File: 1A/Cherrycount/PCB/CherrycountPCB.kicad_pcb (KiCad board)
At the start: 2 copper layers, 105.4 x 64.8 mm, 22 parts, among them J1 Conn_01x02_Female, J2 Conn_01x03_Female, J3 Conn_01x05_Female, J4 Screw_Terminal_01x02, J5 Screw_Terminal_01x02, Q1 2SA1015, Q2 2SA1015

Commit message: Version finale du PCB de compteur de cerises
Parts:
- added G***: LOGO, 7seg:Logo, B.Cu at (172.7, 74.9)
- added J4: Screw_Terminal_01x02, TerminalBlock:TerminalBlock_bornier-2_P5.08mm, F.Cu at (189.2, 87.6)
- renumbered J4 to J5, J5 to J6
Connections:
- F1 pad 1: Net-(J4-Pad1) -> Net-(F1-Pad1)
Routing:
- net Net-(F1-Pad1): track 0.00 -> 15.7 mm
- net Net-(J4-Pad1): track 11.3 -> 10.8 mm
- added copper zone on B.Cu, net GND
- added copper zone on F.Cu, net GND
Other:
- board size 105.4 x 64.8 mm -> 105.4 x 66 mm
- board text added: "GND"
- board text added: "VIN"

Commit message: Version finale du PCB du compteur de cerises
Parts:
- moved A1 7.62 mm to (148.0, 115.6)
- moved AFF1 7.62 mm to (138.9, 74.6)
- moved AFF2 7.62 mm to (163.0, 74.6)
- moved D1 7.62 mm to (182.9, 118.3)
- moved G*** 7.62 mm to (180.3, 74.9)
- moved J1 7.62 mm to (130.8, 123.3)
- moved J2 7.62 mm to (115.6, 123.3)
- moved J3 7.62 mm to (143.5, 123.3)
- moved J4 7.62 mm to (196.8, 87.6)
- moved J5 7.62 mm to (195.6, 97.9)
- moved J6 7.62 mm to (195.6, 111.8)
- moved Q2 7.62 mm to (179.1, 96.0)
- moved R10 7.62 mm to (181.6, 90.0)
- moved R3 7.62 mm to (123.8, 72.5)
- moved R6 7.62 mm to (142.2, 86.7)
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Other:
- outline, holes or cut-outs redrawn

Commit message: Version finale du PCB de compteur de cerises
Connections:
- J3 pad 4: GND -> VIN
- J3 pad 5: VIN -> GND
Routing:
- net VIN: track 87.2 -> 87.8 mm
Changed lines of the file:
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@@
       (net 5 "Net-(A1-Pad5)") (pinfunction "Pin_3") (pintype "passive"))
     (pad "4" thru_hole oval (at 0 7.62 90) (size 1.7 1.7) (drill 1) (layers *.Cu *.Mask)
-      (net 6 "GND") (pinfunction "Pin_4") (pintype "passive"))
+      (net 8 "VIN") (pinfunction "Pin_4") (pintype "passive"))
     (pad "5" thru_hole oval (at 0 10.16 90) (size 1.7 1.7) (drill 1) (layers *.Cu *.Mask)
-      (net 8 "VIN") (pinfunction "Pin_5") (pintype "passive"))
+      (net 6 "GND") (pinfunction "Pin_5") (pintype "passive"))
     (model "${KICAD6_3DMODEL_DIR}/Connector_PinHeader_2.54mm.3dshapes/PinHeader_1x05_P2.54mm_Vertical.wrl"
       (offset (xyz 0 0 0))
@@
   (gr_circle (center 195.58 69.85) (end 197.08 69.85) (layer "Edge.Cuts") (width 0.1) (fill none))
   (gr_circle (center 102.87 69.85) (end 104.37 69.85) (layer "Edge.Cuts") (width 0.1) (fill none))
-  (gr_text "GND" (at 151.13 127) (layer "F.SilkS")
+  (gr_text "GND" (at 153.67 127) (layer "F.SilkS")
     (effects (font (size 0.8 0.8) (thickness 0.125)))
   )
@@
     (effects (font (size 0.8 0.8) (thickness 0.125)))
   )
-  (gr_text "VIN" (at 153.67 127) (layer "F.SilkS")
+  (gr_text "VIN" (at 151.13 127) (layer "F.SilkS")
     (effects (font (size 0.8 0.8) (thickness 0.125)))
   )
@@
   (segment (start 142.24 125.795) (end 137.795 121.35) (width 0.25) (layer "B.Cu") (net 5))
   (segment (start 137.795 121.35) (end 137.795 115.635) (width 0.25) (layer "B.Cu") (net 5))
+  (segment (start 166.305 123.255) (end 153.67 123.255) (width 0.25) (layer "F.Cu") (net 6))
   (segment (start 121.905 124.525) (end 132.08 124.525) (width 0.25) (layer "F.Cu") (net 6))
-  (segment (start 170.02 118.335) (end 182.88 118.335) (width 0.25) (layer "F.Cu") (net 6))
-  (segment (start 163.83 124.525) (end 170.02 118.335) (width 0.25) (layer "F.Cu") (net 6))
+  (segment (start 151.195 125.73) (end 153.67 123.255) (width 0.25) (layer "F.Cu") (net 6))
+  (segment (start 182.88 118.335) (end 171.225 118.335) (width 0.25) (layer "F.Cu") (net 6))
   (segment (start 135.255 121.35) (end 135.255 115.635) (width 0.25) (layer "F.Cu") (net 6))
+  (segment (start 139.635 125.73) (end 151.195 125.73) (width 0.25) (layer "F.Cu") (net 6))
   (segment (start 195.58 116.905) (end 184.31 116.905) (width 0.25) (layer "F.Cu") (net 6))
-  (segment (start 151.13 123.255) (end 152.4 124.525) (width 0.25) (layer "F.Cu") (net 6))
   (segment (start 133.35 123.255) (end 135.255 121.35) (width 0.25) (layer "F.Cu") (net 6))
   (segment (start 184.31 116.905) (end 182.88 118.335) (width 0.25) (layer "F.Cu") (net 6))
-  (segment (start 152.4 124.525) (end 163.83 124.525) (width 0.25) (layer "F.Cu") (net 6))
   (segment (start 120.635 123.255) (end 121.905 124.525) (width 0.25) (layer "F.Cu") (net 6))
   (segment (start 132.08 124.525) (end 133.35 123.255) (width 0.25) (layer "F.Cu") (net 6))
-  (segment (start 135.255 121.35) (end 138.43 124.525) (width 0.25) (layer "F.Cu") (net 6))
-  (segment (start 138.43 124.525) (end 149.86 124.525) (width 0.25) (layer "F.Cu") (net 6))
-  (segment (start 149.86 124.525) (end 151.13 123.255) (width 0.25) (layer "F.Cu") (net 6))
+  (segment (start 171.225 118.335) (end 166.305 123.255) (width 0.25) (layer "F.Cu") (net 6))
+  (segment (start 135.255 121.35) (end 139.635 125.73) (width 0.25) (layer "F.Cu") (net 6))
   (segment (start 182.88 110.715) (end 185.42 108.175) (width 0.25) (layer "F.Cu") (net 8))
-  (segment (start 161.29 115.635) (end 175.26 115.635) (width 0.25) (layer "F.Cu") (net 8))
-  (segment (start 130.175 113.73) (end 130.175 115.635) (width 0.25) (layer "F.Cu") (net 8))
-  (segment (start 130.81 113.095) (end 130.175 113.73) (width 0.25) (layer "F.Cu") (net 8))
-  (segment (start 153.67 123.255) (end 148.59 118.175) (width 0.25) (layer "F.Cu") (net 8))
+  (segment (start 134.62 113.03) (end 130.81 113.03) (width 0.25) (layer "F.Cu") (net 8))
+  (segment (start 180.565 110.715) (end 175.71 115.57) (width 0.25) (layer "F.Cu") (net 8))
+  (segment (start 136.38 114.79) (end 134.62 113.03) (width 0.25) (layer "F.Cu") (net 8))
+  (segment (start 182.88 110.715) (end 180.565 110.715) (width 0.25) (layer "F.Cu") (net 8))
+  (segment (start 175.71 115.57) (end 156.21 115.57) (width 0.25) (layer "F.Cu") (net 8))
+  (segment (start 136.38 116.100991) (end 136.38 114.79) (width 0.25) (layer "F.Cu") (net 8))
   (segment (start 121.905 119.445) (end 127 119.445) (width 0.25) (layer "F.Cu") (net 8))
-  (segment (start 134.62 113.095) (end 130.81 113.095) (width 0.25) (layer "F.Cu") (net 8))
-  (segment (start 180.18 110.715) (end 182.88 110.715) (width 0.25) (layer "F.Cu") (net 8))
+  (segment (start 151.13 120.65) (end 151.13 123.255) (width 0.25) (layer "F.Cu") (net 8))
+  (segment (start 130.175 113.665) (end 130.175 115.635) (width 0.25) (layer "F.Cu") (net 8))
+  (segment (start 151.13 120.65) (end 140.929009 120.65) (width 0.25) (layer "F.Cu") (net 8))
   (segment (start 118.095 123.255) (end 121.905 119.445) (width 0.25) (layer "F.Cu") (net 8))
-  (segment (start 175.26 115.635) (end 180.18 110.715) (width 0.25) (layer "F.Cu") (net 8))
   (segment (start 127 119.445) (end 130.175 116.27) (width 0.25) (layer "F.Cu") (net 8))
+  (segment (start 140.929009 120.65) (end 136.38 116.100991) (width 0.25) (layer "F.Cu") (net 8))
   (segment (start 185.42 108.175) (end 185.42 105.185) (width 0.25) (layer "F.Cu") (net 8))
-  (segment (start 148.59 118.175) (end 138.43 118.175) (width 0.25) (layer "F.Cu") (net 8))
-  (segment (start 136.38 116.125) (end 136.38 114.855) (width 0.25) (layer "F.Cu") (net 8))
-  (segment (start 153.67 123.255) (end 161.29 115.635) (width 0.25) (layer "F.Cu") (net 8))
-  (segment (start 138.43 118.175) (end 136.38 116.125) (width 0.25) (layer "F.Cu") (net 8))
+  (segment (start 130.81 113.03) (end 130.175 113.665) (width 0.25) (layer "F.Cu") (net 8))
+  (segment (start 156.21 115.57) (end 151.13 120.65) (width 0.25) (layer "F.Cu") (net 8))
   (segment (start 130.175 116.27) (end 130.175 115.635) (width 0.25) (layer "F.Cu") (net 8))
-  (segment (start 136.38 114.855) (end 134.62 113.095) (width 0.25) (layer "F.Cu") (net 8))
   (segment (start 116.06 122.75) (end 116.06 112.315) (width 0.25) (layer "B.Cu") (net 16))
   (segment (start 116.06 112.315) (end 102.87 99.125) (width 0.25) (layer "B.Cu") (net 16))

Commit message: Version finale du PCB de compteur de cerises
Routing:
- net D12: track 89.2 -> 90.7 mm
- net Net-(AFF1-Pad10): track 115.8 -> 116.8 mm
- net Net-(A1-Pad28): track 28.0 -> 28.9 mm
- net DP: track 41.5 -> 42.2 mm
- net Net-(AFF1-Pad6): track 56.6 -> 57.2 mm
- net GND: vias 0 -> 3

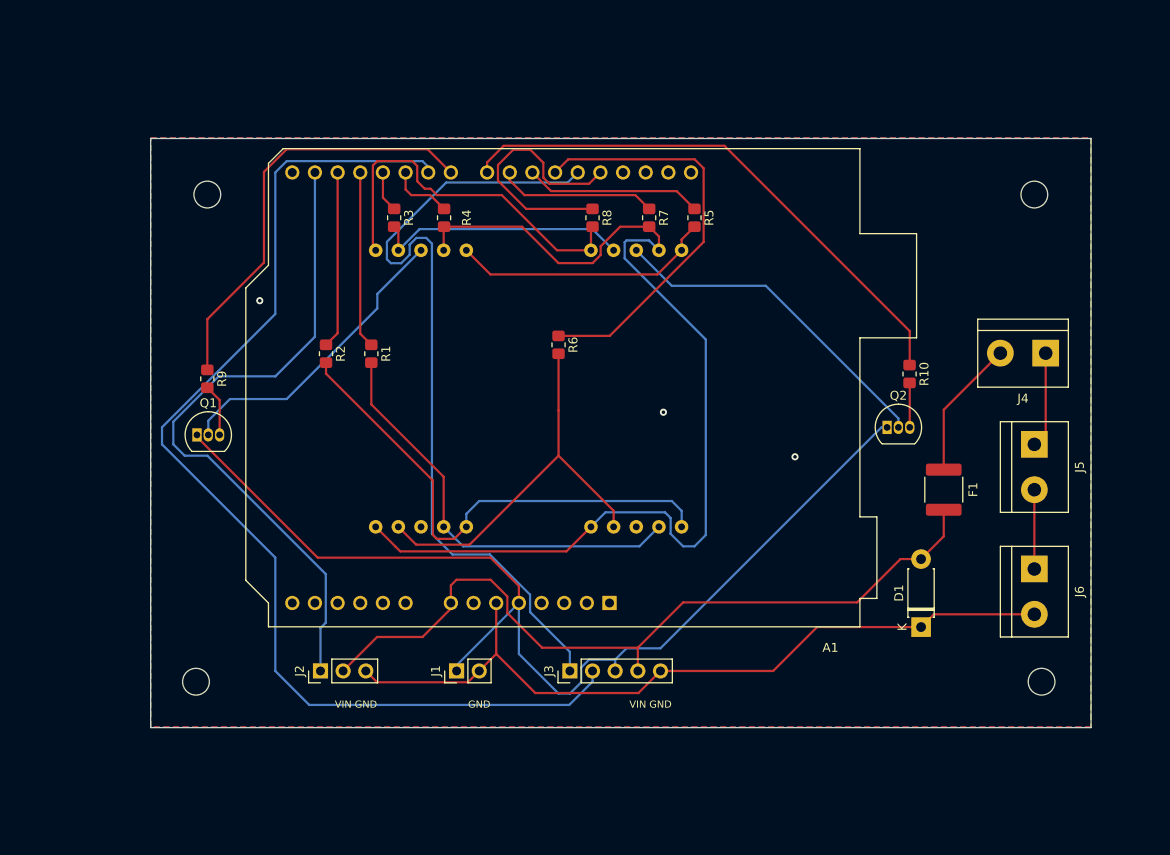
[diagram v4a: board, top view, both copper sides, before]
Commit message: Correction du code Arduino & PCB Cherrycount
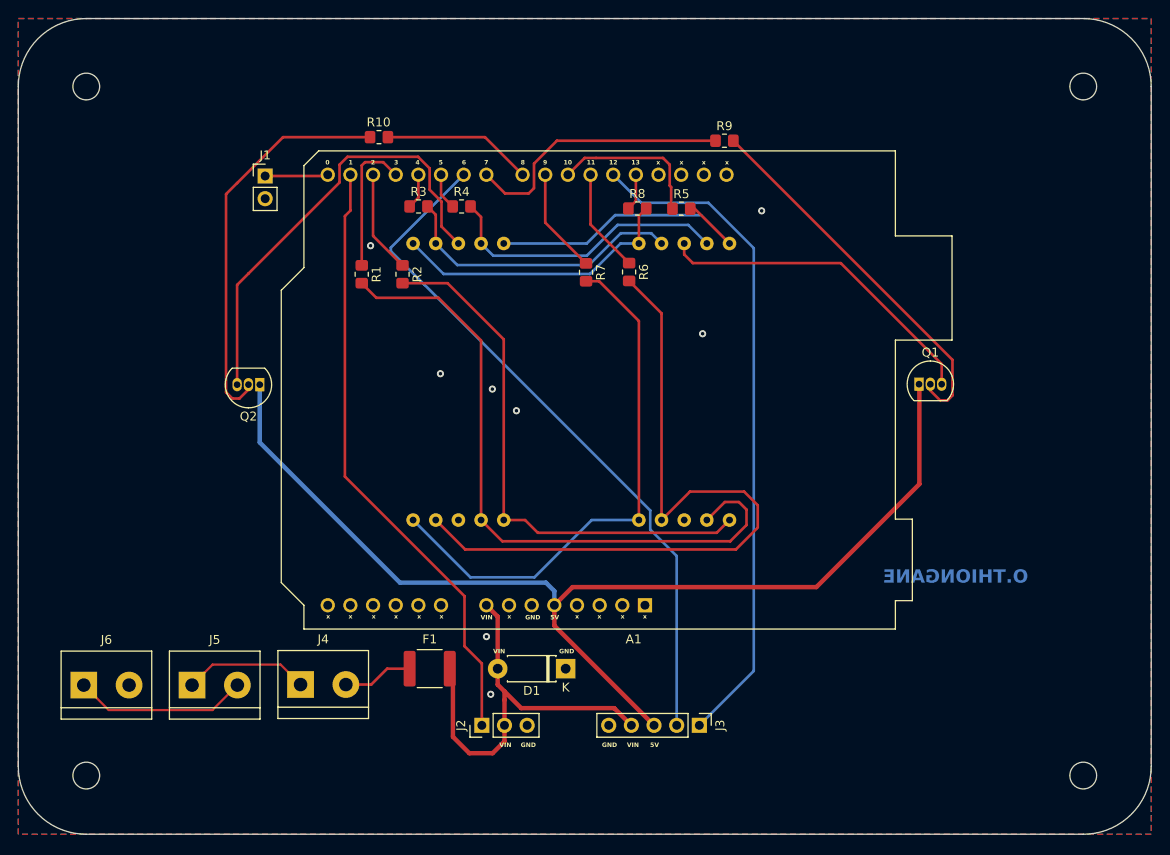
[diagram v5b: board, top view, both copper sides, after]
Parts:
- A1: value Arduino_UNO_R3 -> Arduino_Leonardo
- D1: value DIODE -> type="D" model="DIODE" lib=""
- Q1, Q2: value 2SA1015 -> S8550
- moved J6 107.4 mm to (89.0, 124.8), turned to 0 degrees
- moved J5 98.2 mm to (101.2, 124.8), turned to 0 degrees
- moved J4 91.4 mm to (113.3, 124.8), turned to 0 degrees
- moved Q1 81.1 mm to (182.7, 91.1)
- moved Q2 70.5 mm to (108.8, 91.2), turned to 180 degrees
- moved R10 65.1 mm to (122.1, 63.4), turned to 180 degrees
- moved R9 63.8 mm to (160.8, 63.8), turned to 0 degrees
- moved F1 61.0 mm to (127.8, 123.0), turned to 0 degrees
- moved J1 59.5 mm to (109.4, 67.8), turned to 0 degrees
- moved D1 40.1 mm to (143.0, 123.0), turned to 180 degrees
- moved AFF1 29.5 mm to (168.4, 73.8)
- moved AFF2 20.0 mm to (143.1, 73.8)
- moved J2 19.1 mm to (133.6, 129.3)
- moved J3 15.7 mm to (158.0, 129.3), turned to -90 degrees
- moved G*** 13.5 mm to (190.5, 66.0)
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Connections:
- A1 pad 15: unconnected-(A1-Pad15) -> Net-(A1-D0/RX)
- A1 pad 5: Net-(A1-Pad5) -> Net-(A1-+5V)
- AFF1 pad 10: Net-(AFF1-Pad10) -> Net-(AFF1-g)
- AFF1 pad 2: Net-(AFF1-Pad10) -> Net-(AFF1-d)
- AFF1 pad 3: Net-(AFF1-Pad3) -> Net-(Q1-C)
- AFF2 pad 10: Net-(AFF1-Pad10) -> Net-(AFF1-g)
- AFF2 pad 2: Net-(AFF1-Pad10) -> Net-(AFF1-d)
- AFF2 pad 3: Net-(AFF2-Pad3) -> Net-(Q2-C)
- J1 pad 1: Net-(A1-Pad5) -> Net-(A1-D0/RX)
- J3 pad 3: Net-(A1-Pad5) -> Net-(A1-+5V)
- Q1 pad 1: Net-(A1-Pad5) -> Net-(A1-+5V)
- Q1 pad 2: Net-(AFF1-Pad3) -> Net-(Q1-B)
- Q1 pad 3: Net-(Q1-Pad3) -> Net-(Q1-C)
- Q2 pad 1: Net-(A1-Pad5) -> Net-(A1-+5V)
- Q2 pad 2: Net-(AFF2-Pad3) -> Net-(Q2-B)
- Q2 pad 3: Net-(Q2-Pad3) -> Net-(Q2-C)
- R10 pad 2: Net-(Q2-Pad3) -> Net-(Q2-B)
- R4 pad 2: Net-(AFF1-Pad10) -> Net-(AFF1-d)
- R7 pad 2: Net-(AFF1-Pad10) -> Net-(AFF1-g)
- R9 pad 2: Net-(Q1-Pad3) -> Net-(Q1-B)
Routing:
- net Net-(A1-+5V): track 0.00 -> 123.8 mm
- net Net-(A1-Pad5): track 119.1 -> 0.00 mm
- net Net-(AFF1-Pad10): track 116.8 -> 0.00 mm
- net GND: track 88.0 -> 0.00 mm, vias 3 -> 8
- net Net-(AFF1-g): track 0.00 -> 60.7 mm
- net Net-(Q2-C): track 0.00 -> 50.2 mm
- net D6: track 124.4 -> 78.4 mm
- net BASE2: track 61.7 -> 16.8 mm
- net Net-(Q2-B): track 0.00 -> 44.8 mm
- net Net-(Q1-B): track 0.00 -> 42.6 mm
- net VIN: track 88.1 -> 46.8 mm
- net Net-(AFF2-Pad3): track 38.2 -> 0.00 mm
- net Net-(Q1-C): track 0.00 -> 37.4 mm
- net Net-(AFF1-f): track 44.9 -> 82.0 mm
- net Net-(A1-D11): track 46.6 -> 11.7 mm
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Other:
- board size 105.4 x 66 mm -> 127 x 91.4 mm
- board text added: "0"
- board text added: "1"
- board text added: "10"
- board text added: "11"
- board text added: "12"
- board text added: "13"
- board text added: "2"
- board text added: "3"
- board text added: "4"
- board text added: "5"
- board text added: "5V"
- board text added: "6"
- board text added: "7"
- board text added: "8"
- board text added: "9"
- board text added: "ARES"
- board text added: "Cherrycount"
- board text added: "ENSEA"
- board text added: "O.THIONGANE"
- board text added: "x"

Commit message: Correction du code Arduino & PCB Cherrycount
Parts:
- added R11: 1M, Resistor_SMD:R_0805_2012Metric_Pad1.20x1.40mm_HandSolder, F.Cu at (112.5, 68.8)
- moved J1 1.08 mm to (108.3, 67.8)
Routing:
- net Net-(Q2-B): track 44.8 -> 46.8 mm
- net Net-(A1-D0/RX): track 7.08 -> 8.36 mm
- net GND: vias 8 -> 13
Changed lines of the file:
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@@
+  )
+  (footprint "Resistor_SMD:R_0805_2012Metric_Pad1.20x1.40mm_HandSolder" (layer "F.Cu")
+    (at 112.51 68.76 90)
+    (descr "Resistor SMD 0805 (2012 Metric), square (rectangular) end terminal, IPC_7351 nominal with elongated pad for handsoldering. (Body size source: IPC-SM-782 page 72, https://www.pcb-3d.com/wordpress/wp-content/uploads/ipc-sm-782a_amendment_1_and_2.pdf), generated with kicad-footprint-generator")
+    (tags "resistor handsolder")
+    (property "Sheetfile" "CherrycountPCB.kicad_sch")
+    (property "Sheetname" "")
+    (property "ki_description" "Resistor")
+    (property "ki_keywords" "R res resistor")
+    (attr smd)
+    (fp_text reference "R11" (at 0 -1.65 90) (layer "F.SilkS")
+        (effects (font (size 1 1) (thickness 0.15)))
+    )
+    (fp_text value "1M" (at 0 1.65 90) (layer "F.Fab")
+        (effects (font (size 1 1) (thickness 0.15)))
+    )
+    (fp_text user "${REFERENCE}" (at 0 0 90) (layer "F.Fab")
+        (effects (font (size 0.5 0.5) (thickness 0.08)))
+    )
+    (fp_line (start -0.227064 -0.735) (end 0.227064 -0.735)
+      (stroke (width 0.12) (type solid)) (layer "F.SilkS"))
+    (fp_line (start -0.227064 0.735) (end 0.227064 0.735)
+      (stroke (width 0.12) (type solid)) (layer "F.SilkS"))
+    (fp_line (start -1.85 -0.95) (end 1.85 -0.95)
+      (stroke (width 0.05) (type solid)) (layer "F.CrtYd"))
+    (fp_line (start -1.85 0.95) (end -1.85 -0.95)
+      (stroke (width 0.05) (type solid)) (layer "F.CrtYd"))
+    (fp_line (start 1.85 -0.95) (end 1.85 0.95)
+      (stroke (width 0.05) (type solid)) (layer "F.CrtYd"))
+    (fp_line (start 1.85 0.95) (end -1.85 0.95)
+      (stroke (width 0.05) (type solid)) (layer "F.CrtYd"))
+    (fp_line (start -1 -0.625) (end 1 -0.625)
+      (stroke (width 0.1) (type solid)) (layer "F.Fab"))
+    (fp_line (start -1 0.625) (end -1 -0.625)
+      (stroke (width 0.1) (type solid)) (layer "F.Fab"))
+    (fp_line (start 1 -0.625) (end 1 0.625)
+      (stroke (width 0.1) (type solid)) (layer "F.Fab"))
+    (fp_line (start 1 0.625) (end -1 0.625)
+      (stroke (width 0.1) (type solid)) (layer "F.Fab"))
+    (pad "1" smd roundrect (at -1 0 90) (size 1.2 1.4) (layers "F.Cu" "F.Paste" "F.Mask") (roundrect_rratio 0.208333)
+      (net 1 "GND") (pintype "passive"))
+    (pad "2" smd roundrect (at 1 0 90) (size 1.2 1.4) (layers "F.Cu" "F.Paste" "F.Mask") (roundrect_rratio 0.208333)
+      (net 21 "Net-(A1-D0{slash}RX)") (pintype "passive"))
+    (model "${KICAD6_3DMODEL_DIR}/Resistor_SMD.3dshapes/R_0805_2012Metric.wrl"
+      (offset (xyz 0 0 0))
+      (scale (xyz 1 1 1))
+      (rotate (xyz 0 0 0))
+    )
   )
   (footprint "Resistor_SMD:R_0805_2012Metric_Pad1.20x1.40mm_HandSolder" (layer "F.Cu")
@@
   )
   (footprint "Connector_PinHeader_2.54mm:PinHeader_1x02_P2.54mm_Vertical" (layer "F.Cu")
-    (at 109.352 67.772)
+    (at 108.27 67.76)
     (descr "Through hole straight pin header, 1x02, 2.54mm pitch, single row")
     (tags "Through hole pin header THT 1x02 2.54mm single row")
@@
     (effects (font (size 0.5 0.5) (thickness 0.1) bold) (justify left bottom))
   )
+  (via (at 123.05 71.19) (size 0.8) (drill 0.4) (layers "F.Cu" "B.Cu") (free) (net 1))
+  (via (at 153.38 69.72) (size 0.8) (drill 0.4) (layers "F.Cu" "B.Cu") (free) (net 1))
   (via (at 121.172 75.587) (size 0.8) (drill 0.4) (layers "F.Cu" "B.Cu") (free) (net 1))
   (via (at 158.392 85.457) (size 0.8) (drill 0.4) (layers "F.Cu" "B.Cu") (free) (net 1))
@@
   (via (at 165.012 71.677) (size 0.8) (drill 0.4) (layers "F.Cu" "B.Cu") (free) (net 1))
   (via (at 134.822 91.657) (size 0.8) (drill 0.4) (layers "F.Cu" "B.Cu") (free) (net 1))
+  (via (at 147.76 70.72) (size 0.8) (drill 0.4) (layers "F.Cu" "B.Cu") (free) (net 1))
+  (via (at 132 125.78) (size 0.8) (drill 0.4) (layers "F.Cu" "B.Cu") (free) (net 1))
+  (via (at 152.53 85.07) (size 0.8) (drill 0.4) (layers "F.Cu" "B.Cu") (free) (net 1))
   (via (at 129.002 89.937) (size 0.8) (drill 0.4) (layers "F.Cu" "B.Cu") (free) (net 1))
   (via (at 134.162 119.407) (size 0.8) (drill 0.4) (layers "F.Cu" "B.Cu") (free) (net 1))
@@
   (segment (start 158.026 129.35) (end 164.122 123.254) (width 0.3) (layer "B.Cu") (net 20))
   (segment (start 151.519 70.777) (end 148.37 67.628) (width 0.3) (layer "B.Cu") (net 20))
-  (segment (start 109.352 67.772) (end 116.226 67.772) (width 0.3) (layer "F.Cu") (net 21))
+  (segment (start 108.27 67.76) (end 112.51 67.76) (width 0.25) (layer "F.Cu") (net 21))
+  (segment (start 112.51 67.76) (end 112.642 67.628) (width 0.25) (layer "F.Cu") (net 21))
+  (segment (start 112.642 67.628) (end 116.37 67.628) (width 0.25) (layer "F.Cu") (net 21))
   (segment (start 116.226 67.772) (end 116.37 67.628) (width 0.3) (layer "F.Cu") (net 21))
   (segment (start 121.45 74.486) (end 121.45 67.628) (width 0.3) (layer "F.Cu") (net 22))
@@
   (segment (start 183.92 91.83) (end 183.92 91.11) (width 0.25) (layer "F.Cu") (net 48))
   (segment (start 186.4 92.37) (end 185.85 92.92) (width 0.3) (layer "F.Cu") (net 48))
-  (segment (start 106.21 68.564) (end 106.206 68.564) (width 0.25) (layer "F.Cu") (net 49))
-  (segment (start 104.97 92.01) (end 105.68 92.72) (width 0.3) (layer "F.Cu") (net 49))
-  (segment (start 105.68 92.72) (end 106.47 92.72) (width 0.3) (layer "F.Cu") (net 49))
-  (segment (start 104.97 69.8) (end 104.97 92.01) (width 0.3) (layer "F.Cu") (net 49))
-  (segment (start 106.21 68.564) (end 111.357 63.417) (width 0.3) (layer "F.Cu") (net 49))
-  (segment (start 106.47 92.72) (end 107.48 91.71) (width 0.3) (layer "F.Cu") (net 49))
-  (segment (start 106.206 68.564) (end 104.97 69.8) (width 0.3) (layer "F.Cu") (net 49))
-  (segment (start 107.48 91.71) (end 107.48 91.16) (width 0.3) (layer "F.Cu") (net 49))
-  (segment (start 111.357 63.417) (end 121.112 63.417) (width 0.3) (layer "F.Cu") (net 49))
+  (segment (start 104.97 66.31) (end 107.863 63.417) (width 0.3) (layer "F.Cu") (net 49))
+  (segment (start 105.68 92.72) (end 104.97 92.01) (width 0.3) (layer "F.Cu") (net 49))
+  (segment (start 106.47 92.72) (end 105.68 92.72) (width 0.3) (layer "F.Cu") (net 49))
+  (segment (start 107.863 63.417) (end 121.112 63.417) (width 0.3) (layer "F.Cu") (net 49))
+  (segment (start 107.48 91.71) (end 106.47 92.72) (width 0.3) (layer "F.Cu") (net 49))
+  (segment (start 104.97 92.01) (end 104.97 66.31) (width 0.3) (layer "F.Cu") (net 49))
+  (segment (start 107.48 91.16) (end 107.48 91.71) (width 0.3) (layer "F.Cu") (net 49))
   (zone (net 1) (net_name "GND") (layer "F.Cu") (hatch edge 0.5)
     (connect_pads (clearance 0.5))
